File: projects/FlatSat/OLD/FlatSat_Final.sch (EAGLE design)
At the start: 34 parts, among them J1 M22-6013005, J2 M22-6013005, J3 M22-6013005, J4 M22-6013005, J5 M22-6013005, J6 M22-6013005

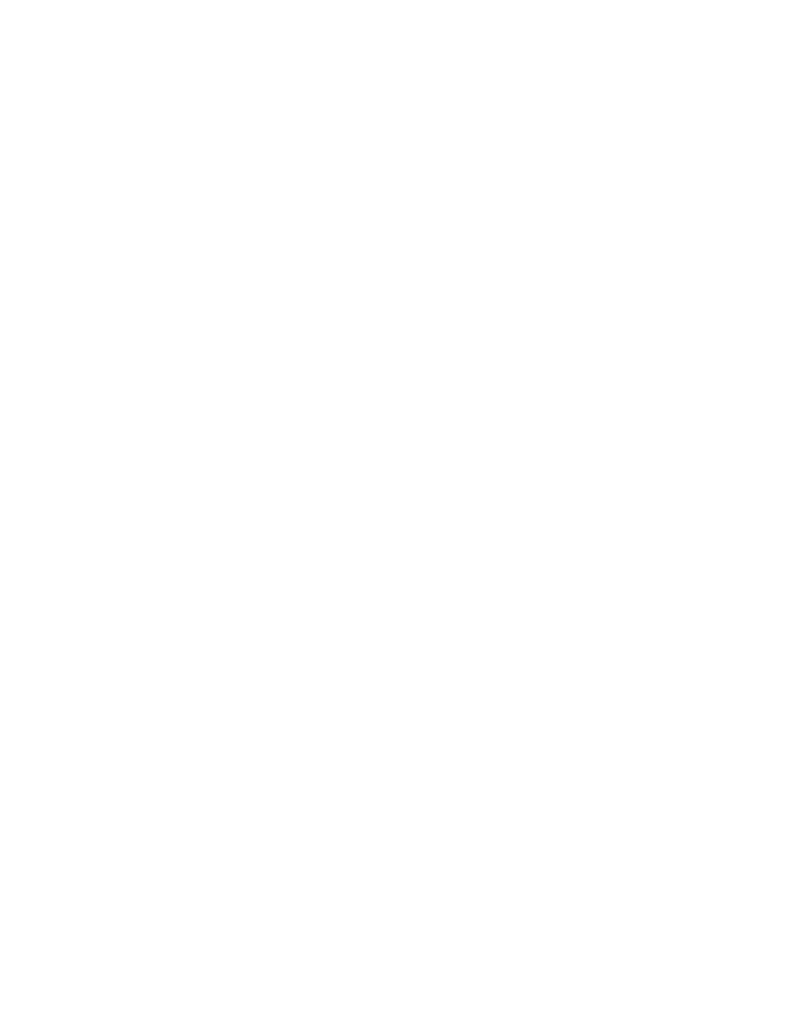
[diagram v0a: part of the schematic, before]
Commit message: Updated PCB desgins to fix wiring mismatches
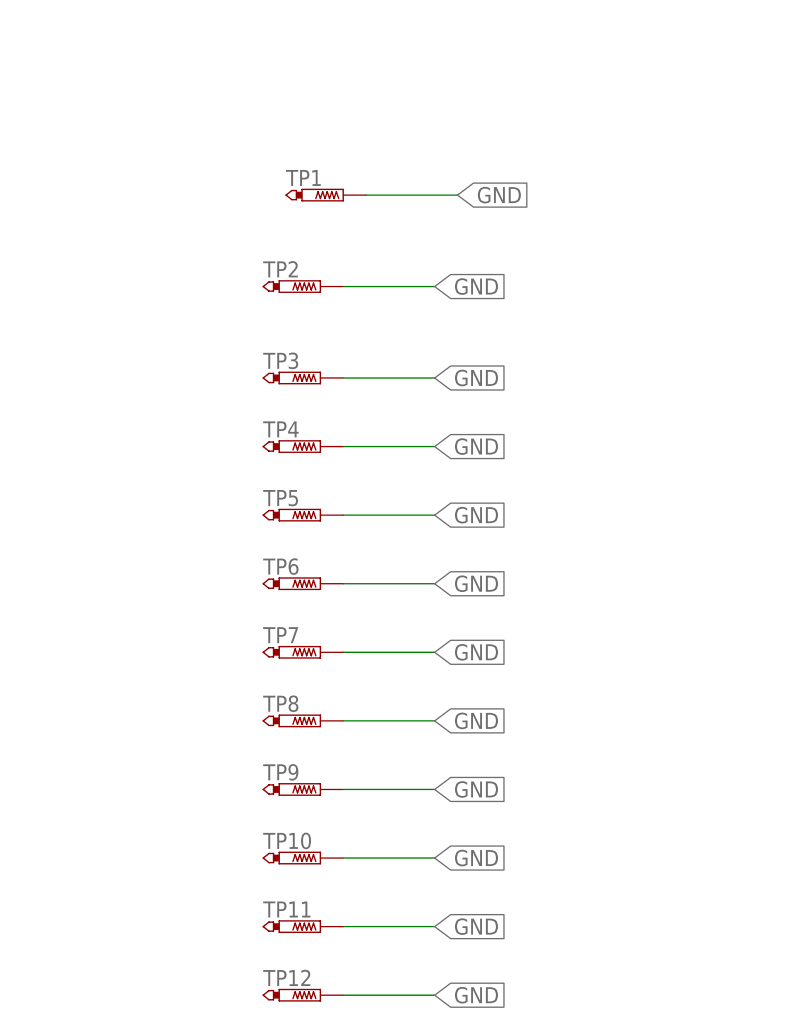
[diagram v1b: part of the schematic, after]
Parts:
- added TP1, TP10, TP11, TP12, TP2, TP3, TP4, TP5, TP6, TP7, TP8, TP9: PTR1PAD1-13, testpad:PTR1PAD1-13
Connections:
- net GND: now also TP1.TP, TP10.TP, TP11.TP, TP12.TP, TP2.TP, TP3.TP, TP4.TP, TP5.TP, TP6.TP, TP7.TP, TP8.TP, TP9.TP
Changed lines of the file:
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@@
 <part name="H22" library="holes" library_urn="urn:adsk.eagle:library:237" deviceset="MOUNT-PAD-ROUND" device="3.2" package3d_urn="urn:adsk.eagle:package:14282/1"/>
 <part name="GND84" library="supply1" library_urn="urn:adsk.eagle:library:371" deviceset="GND" device=""/>
+<part name="TP1" library="testpad" library_urn="urn:adsk.eagle:library:385" deviceset="PTR1" device="PAD1-13" package3d_urn="urn:adsk.eagle:package:27946/1"/>
+<part name="TP2" library="testpad" library_urn="urn:adsk.eagle:library:385" deviceset="PTR1" device="PAD1-13" package3d_urn="urn:adsk.eagle:package:27946/1"/>
+<part name="TP3" library="testpad" library_urn="urn:adsk.eagle:library:385" deviceset="PTR1" device="PAD1-13" package3d_urn="urn:adsk.eagle:package:27946/1"/>
+<part name="TP4" library="testpad" library_urn="urn:adsk.eagle:library:385" deviceset="PTR1" device="PAD1-13" package3d_urn="urn:adsk.eagle:package:27946/1"/>
+<part name="TP5" library="testpad" library_urn="urn:adsk.eagle:library:385" deviceset="PTR1" device="PAD1-13" package3d_urn="urn:adsk.eagle:package:27946/1"/>
+<part name="TP6" library="testpad" library_urn="urn:adsk.eagle:library:385" deviceset="PTR1" device="PAD1-13" package3d_urn="urn:adsk.eagle:package:27946/1"/>
+<part name="TP7" library="testpad" library_urn="urn:adsk.eagle:library:385" deviceset="PTR1" device="PAD1-13" package3d_urn="urn:adsk.eagle:package:27946/1"/>
+<part name="TP8" library="testpad" library_urn="urn:adsk.eagle:library:385" deviceset="PTR1" device="PAD1-13" package3d_urn="urn:adsk.eagle:package:27946/1"/>
+<part name="TP9" library="testpad" library_urn="urn:adsk.eagle:library:385" deviceset="PTR1" device="PAD1-13" package3d_urn="urn:adsk.eagle:package:27946/1"/>
+<part name="TP10" library="testpad" library_urn="urn:adsk.eagle:library:385" deviceset="PTR1" device="PAD1-13" package3d_urn="urn:adsk.eagle:package:27946/1"/>
+<part name="TP11" library="testpad" library_urn="urn:adsk.eagle:library:385" deviceset="PTR1" device="PAD1-13" package3d_urn="urn:adsk.eagle:package:27946/1"/>
+<part name="TP12" library="testpad" library_urn="urn:adsk.eagle:library:385" deviceset="PTR1" device="PAD1-13" package3d_urn="urn:adsk.eagle:package:27946/1"/>
 </parts>
 <sheets>
@@
 <attribute name="VALUE" x="-147.32" y="457.2" size="1.778" layer="96" rot="R270"/>
 </instance>
+<instance part="TP1" gate="G$1" x="-414.02" y="441.96" smashed="yes" rot="R270">
+<attribute name="NAME" x="-420.37" y="442.976" size="1.778" layer="95"/>
+<attribute name="TP_SIGNAL_NAME" x="-416.56" y="440.69" size="1.778" layer="97" rot="R270"/>
+</instance>
+<instance part="TP2" gate="G$1" x="-416.56" y="431.8" smashed="yes" rot="R270">
+<attribute name="NAME" x="-422.91" y="432.816" size="1.778" layer="95"/>
+<attribute name="TP_SIGNAL_NAME" x="-419.1" y="430.53" size="1.778" layer="97" rot="R270"/>
+</instance>
+<instance part="TP3" gate="G$1" x="-416.56" y="421.64" smashed="yes" rot="R270">
+<attribute name="NAME" x="-422.91" y="422.656" size="1.778" layer="95"/>
+<attribute name="TP_SIGNAL_NAME" x="-419.1" y="420.37" size="1.778" layer="97" rot="R270"/>
+</instance>
+<instance part="TP4" gate="G$1" x="-416.56" y="414.02" smashed="yes" rot="R270">
+<attribute name="NAME" x="-422.91" y="415.036" size="1.778" layer="95"/>
+<attribute name="TP_SIGNAL_NAME" x="-419.1" y="412.75" size="1.778" layer="97" rot="R270"/>
+</instance>
+<instance part="TP5" gate="G$1" x="-416.56" y="406.4" smashed="yes" rot="R270">
+<attribute name="NAME" x="-422.91" y="407.416" size="1.778" layer="95"/>
+<attribute name="TP_SIGNAL_NAME" x="-419.1" y="405.13" size="1.778" layer="97" rot="R270"/>
+</instance>
+<instance part="TP6" gate="G$1" x="-416.56" y="398.78" smashed="yes" rot="R270">
+<attribute name="NAME" x="-422.91" y="399.796" size="1.778" layer="95"/>
+<attribute name="TP_SIGNAL_NAME" x="-419.1" y="397.51" size="1.778" layer="97" rot="R270"/>
+</instance>
+<instance part="TP7" gate="G$1" x="-416.56" y="391.16" smashed="yes" rot="R270">
+<attribute name="NAME" x="-422.91" y="392.176" size="1.778" layer="95"/>
+<attribute name="TP_SIGNAL_NAME" x="-419.1" y="389.89" size="1.778" layer="97" rot="R270"/>
+</instance>
+<instance part="TP8" gate="G$1" x="-416.56" y="383.54" smashed="yes" rot="R270">
+<attribute name="NAME" x="-422.91" y="384.556" size="1.778" layer="95"/>
+<attribute name="TP_SIGNAL_NAME" x="-419.1" y="382.27" size="1.778" layer="97" rot="R270"/>
+</instance>
+<instance part="TP9" gate="G$1" x="-416.56" y="375.92" smashed="yes" rot="R270">
+<attribute name="NAME" x="-422.91" y="376.936" size="1.778" layer="95"/>
+<attribute name="TP_SIGNAL_NAME" x="-419.1" y="374.65" size="1.778" layer="97" rot="R270"/>
+</instance>
+<instance part="TP10" gate="G$1" x="-416.56" y="368.3" smashed="yes" rot="R270">
+<attribute name="NAME" x="-422.91" y="369.316" size="1.778" layer="95"/>
+<attribute name="TP_SIGNAL_NAME" x="-419.1" y="367.03" size="1.778" layer="97" rot="R270"/>
+</instance>
+<instance part="TP11" gate="G$1" x="-416.56" y="360.68" smashed="yes" rot="R270">
+<attribute name="NAME" x="-422.91" y="361.696" size="1.778" layer="95"/>
+<attribute name="TP_SIGNAL_NAME" x="-419.1" y="359.41" size="1.778" layer="97" rot="R270"/>
+</instance>
+<instance part="TP12" gate="G$1" x="-416.56" y="353.06" smashed="yes" rot="R270">
+<attribute name="NAME" x="-422.91" y="354.076" size="1.778" layer="95"/>
+<attribute name="TP_SIGNAL_NAME" x="-419.1" y="351.79" size="1.778" layer="97" rot="R270"/>
+</instance>
 </instances>
 <busses>
@@
 <pinref part="GND84" gate="1" pin="GND"/>
 </segment>
+<segment>
+<pinref part="TP1" gate="G$1" pin="TP"/>
+<wire x1="-411.48" y1="441.96" x2="-401.32" y2="441.96" width="0.1524" layer="91"/>
+<label x="-401.32" y="441.96" size="1.778" layer="95" xref="yes"/>
+</segment>
+<segment>
+<pinref part="TP2" gate="G$1" pin="TP"/>
+<wire x1="-414.02" y1="431.8" x2="-403.86" y2="431.8" width="0.1524" layer="91"/>
+<label x="-403.86" y="431.8" size="1.778" layer="95" xref="yes"/>
+</segment>
+<segment>
+<pinref part="TP3" gate="G$1" pin="TP"/>
+<wire x1="-414.02" y1="421.64" x2="-403.86" y2="421.64" width="0.1524" layer="91"/>
+<label x="-403.86" y="421.64" size="1.778" layer="95" xref="yes"/>
+</segment>
+<segment>
+<pinref part="TP4" gate="G$1" pin="TP"/>
+<wire x1="-414.02" y1="414.02" x2="-403.86" y2="414.02" width="0.1524" layer="91"/>
+<label x="-403.86" y="414.02" size="1.778" layer="95" xref="yes"/>
+</segment>
+<segment>
+<pinref part="TP5" gate="G$1" pin="TP"/>
+<wire x1="-414.02" y1="406.4" x2="-403.86" y2="406.4" width="0.1524" layer="91"/>
+<label x="-403.86" y="406.4" size="1.778" layer="95" xref="yes"/>
+</segment>
+<segment>
+<pinref part="TP6" gate="G$1" pin="TP"/>
+<wire x1="-414.02" y1="398.78" x2="-403.86" y2="398.78" width="0.1524" layer="91"/>
+<label x="-403.86" y="398.78" size="1.778" layer="95" xref="yes"/>
+</segment>
+<segment>
+<pinref part="TP7" gate="G$1" pin="TP"/>
+<wire x1="-414.02" y1="391.16" x2="-403.86" y2="391.16" width="0.1524" layer="91"/>
+<label x="-403.86" y="391.16" size="1.778" layer="95" xref="yes"/>
+</segment>
+<segment>
+<pinref part="TP8" gate="G$1" pin="TP"/>
+<wire x1="-414.02" y1="383.54" x2="-403.86" y2="383.54" width="0.1524" layer="91"/>
+<label x="-403.86" y="383.54" size="1.778" layer="95" xref="yes"/>
+</segment>
+<segment>
+<pinref part="TP9" gate="G$1" pin="TP"/>
+<wire x1="-414.02" y1="375.92" x2="-403.86" y2="375.92" width="0.1524" layer="91"/>
+<label x="-403.86" y="375.92" size="1.778" layer="95" xref="yes"/>
+</segment>
+<segment>
+<pinref part="TP10" gate="G$1" pin="TP"/>
+<wire x1="-414.02" y1="368.3" x2="-403.86" y2="368.3" width="0.1524" layer="91"/>
+<label x="-403.86" y="368.3" size="1.778" layer="95" xref="yes"/>
+</segment>
+<segment>
+<pinref part="TP11" gate="G$1" pin="TP"/>
+<wire x1="-414.02" y1="360.68" x2="-403.86" y2="360.68" width="0.1524" layer="91"/>
+<label x="-403.86" y="360.68" size="1.778" layer="95" xref="yes"/>
+</segment>
+<segment>
+<pinref part="TP12" gate="G$1" pin="TP"/>
+<wire x1="-414.02" y1="353.06" x2="-403.86" y2="353.06" width="0.1524" layer="91"/>
+<label x="-403.86" y="353.06" size="1.778" layer="95" xref="yes"/>
+</segment>
 </net>
